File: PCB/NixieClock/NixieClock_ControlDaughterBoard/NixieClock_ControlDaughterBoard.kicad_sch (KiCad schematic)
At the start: 35 parts, among them J1 Conn_01x05, J2 Conn_01x05, J3 Conn_01x04_Pin, J4 Conn_01x04_Pin, Q1 IRLML6244, Q2 IRLML6244, Q3 IRLML6402

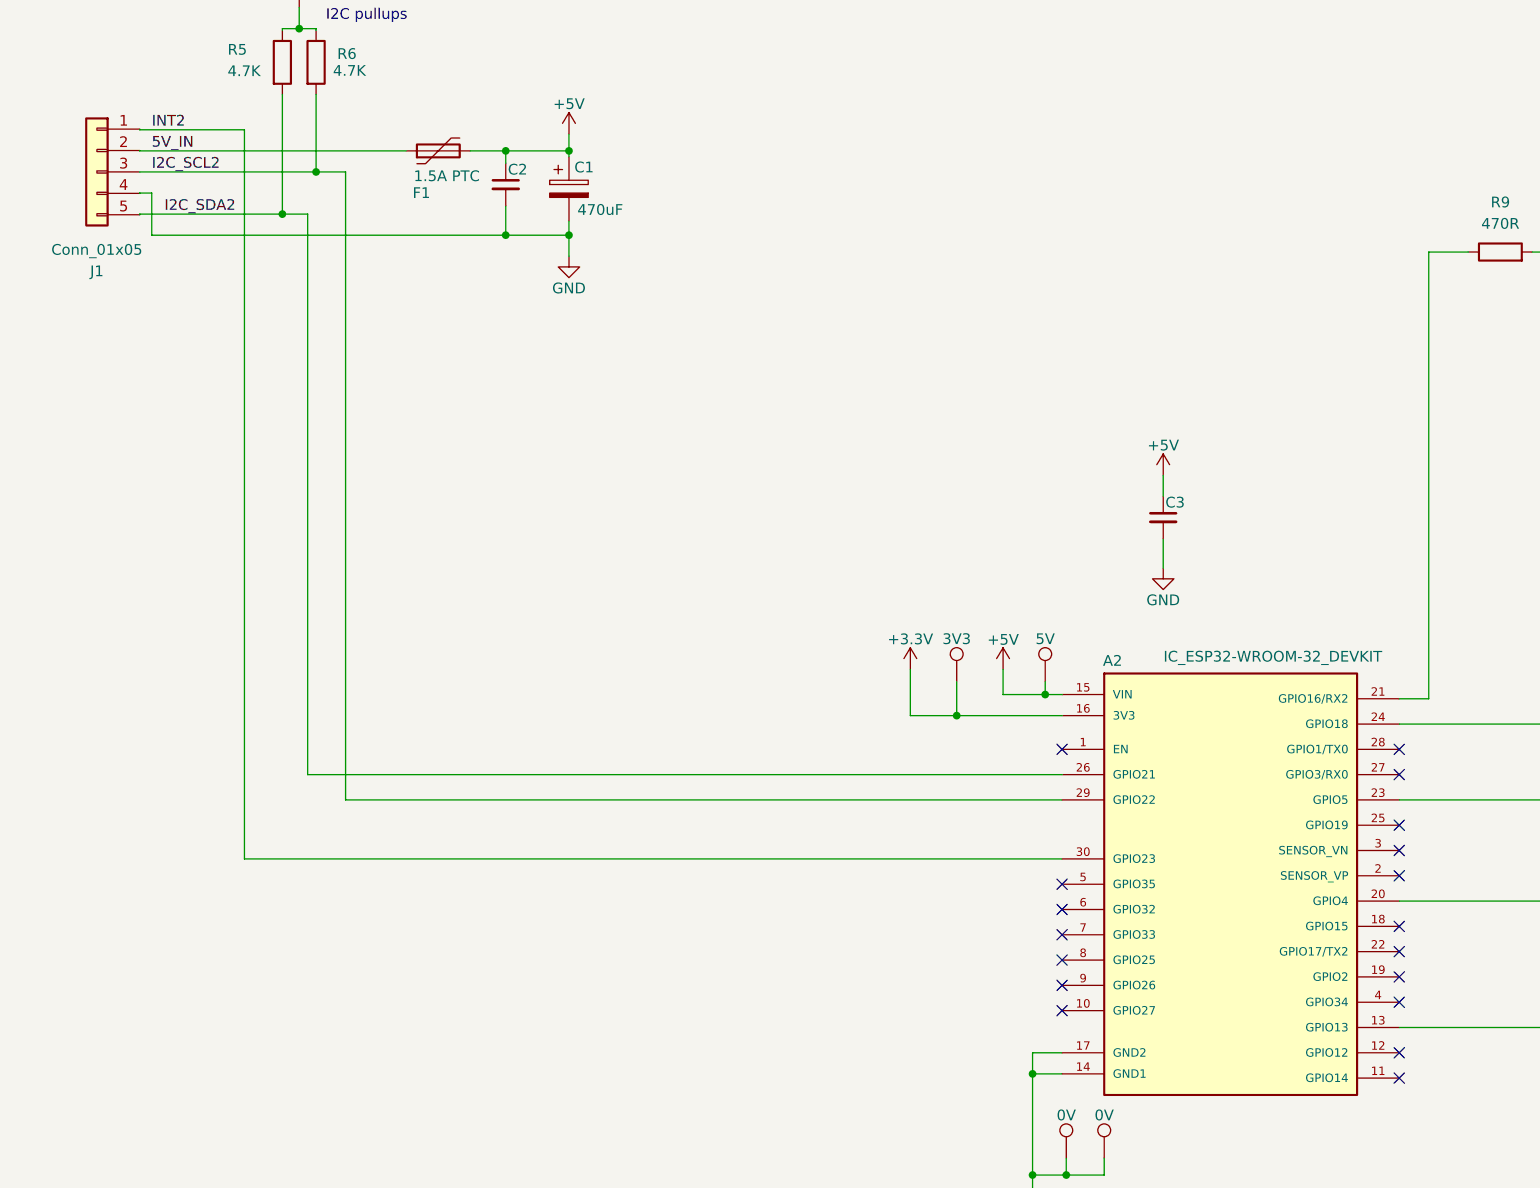
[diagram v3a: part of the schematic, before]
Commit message: PCB layout 2 complete
layout 1 was incorrect as the connectors and LEDs were not located in the right place to correctly mate with the tube panel PCBA. When connectors and LEDs were moved, all the traces became scrambled. it was necessary to re-wire the entire board.
ESP32 pins were also remapped to improve ease of wiring
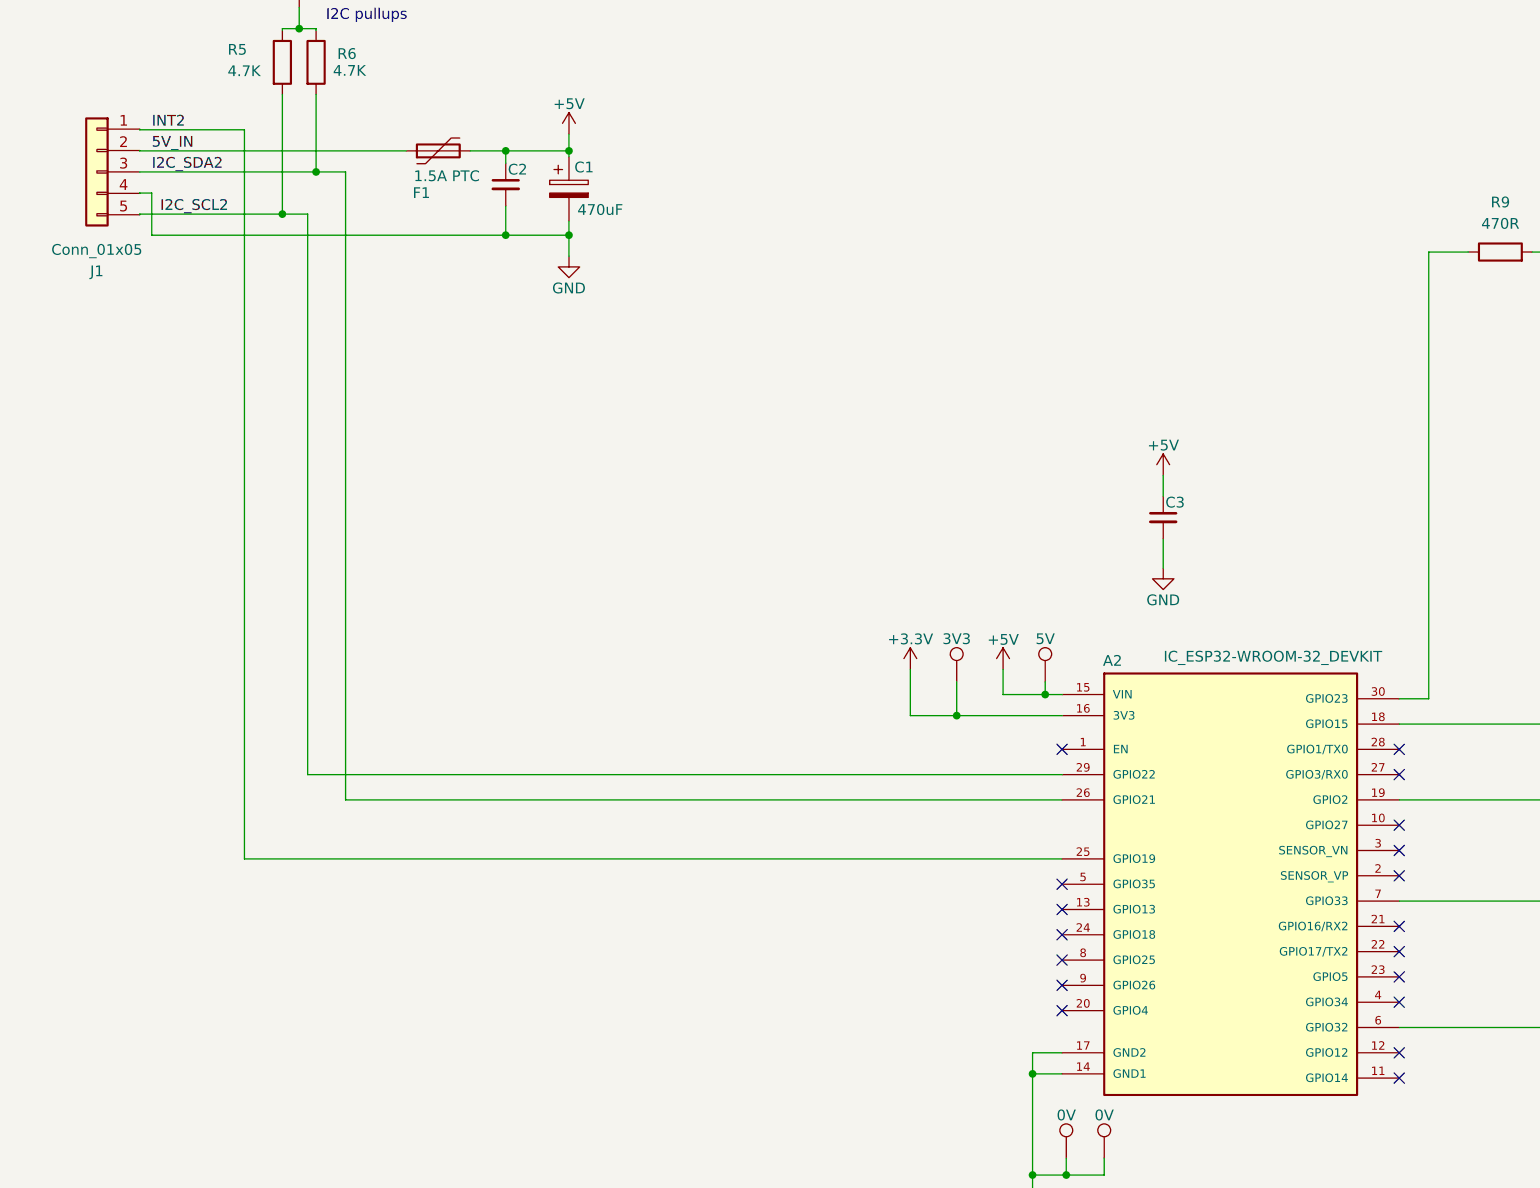
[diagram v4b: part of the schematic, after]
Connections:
- net I2C_SCL1: now also A2.18 (GPIO15); no longer A2.24 (GPIO18)
- net I2C_SCL2: now also J1.5 (Pin_5), R5.2; no longer J1.3 (Pin_3), R6.2
- net I2C_SDA1: now also A2.19 (GPIO2); no longer A2.23 (GPIO5)
- net I2C_SDA2: now also J1.3 (Pin_3), R6.2; no longer J1.5 (Pin_5), R5.2
- net INT2: now also A2.25 (GPIO19); no longer A2.30 (GPIO23)
- net LDR_IN: now also A2.7 (GPIO33); no longer A2.20 (GPIO4)
- net LED-Data_3V3: now also A2.6 (GPIO32); no longer A2.13 (GPIO13)
- net at R9.1: now also A2.30 (GPIO23); no longer A2.21 (GPIO16/RX2)
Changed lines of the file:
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@@
+		)
+	)
+	(label "I2C_SDA2"
+		(at 91 37 0)
+		(effects
+			(font
+				(size 1.27 1.27)
+			)
+			(justify left bottom)
 		)
 	)
@@
 	(label "INT2"
 		(at 91 32 0)
-		(effects
-			(font
-				(size 1.27 1.27)
-			)
-			(justify left bottom)
-		)
-	)
-	(label "I2C_SCL2"
-		(at 91 37 0)
 		(effects
 			(font
@@
 		)
 	)
-	(label "I2C_SCL1"
-		(at 352.5 142.5 0)
+	(label "I2C_SCL2"
+		(at 92 42 0)
 		(effects
 			(font
@@
 		)
 	)
-	(label "I2C_SDA2"
-		(at 92.5 42 0)
+	(label "I2C_SCL1"
+		(at 352.5 142.5 0)
 		(effects
 			(font

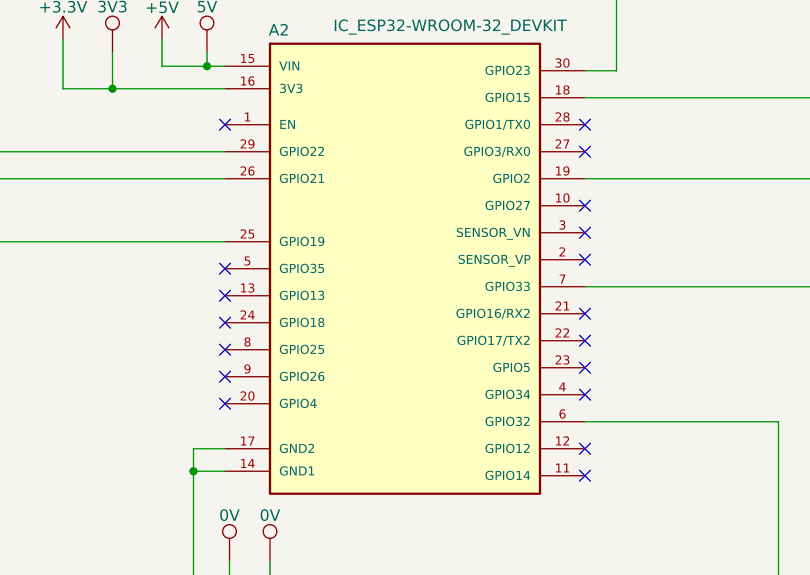
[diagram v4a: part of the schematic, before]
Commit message: I2C pin remap based on breadboard tests
tested I2C pin mappings on breadboard and found that using GPIO2 caused the board to get stuck in boot mode. remapped to adjacent pin GPIO4 for safety.
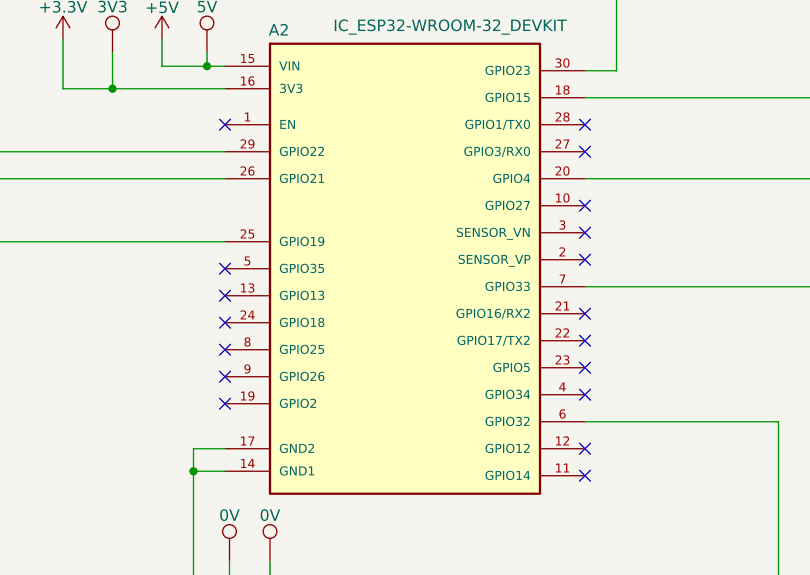
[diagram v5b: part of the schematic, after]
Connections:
- net I2C_SDA1: now also A2.20 (GPIO4); no longer A2.19 (GPIO2)

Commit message: Fill component details and export BOM
filled missing component information, exported BOM
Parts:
- A1: Manufacturer (none) -> Unknown; Manufacturer PN (none) -> ASSY_NCH8200HV; Supplier (none) -> Amazon
- A2: Manufacturer P/N ESP32-WROOM-32_DEVKIT -> (none); Manufacturer PN (none) -> ESP32-WROOM-32_DEVKIT; Supplier Terminal Curiosity -> Amazon
- A3: value ~ -> 4090; Manufacturer (none) -> Adafruit; Manufacturer PN (none) -> 4090; Supplier (none) -> Digikey
- C1: Manufacturer P/N UWT1C471MNL1GS -> (none); Manufacturer PN (none) -> UWT1C471MNL1GS
- C2, C3: Manufacturer P/N CL21B104KCFNNNE -> (none); Manufacturer PN (none) -> CL21B104KCFNNNE
- D1: Manufacturer (none) -> Generic; Manufacturer PN (none) -> PL9823
- D2, D3, D4: Manufacturer (none) -> Generic; Manufacturer PN (none) -> PL9823; Supplier (none) -> Terminal Curiosity
- F1: Manufacturer P/N NANOSMDC150F-2 -> (none); Manufacturer PN (none) -> NANOSMDC150F-2
- J1, J2: Manufacturer (none) -> JST Sales America Inc.; Manufacturer PN (none) -> B5B-XH-A; Supplier (none) -> Digikey
- J3, J4: value Conn_01x04_Pin -> Conn_01x04; Manufacturer (none) -> Sullins Connector Solutions; Manufacturer PN (none) -> PPTC041LFBN-RC; Supplier (none) -> Digikey
- Q1: Manufacturer PN (none) -> IRLML6244TRPBF
- Q2: Manufacturer P/N IRLML6344TRPBF -> (none); Manufacturer PN (none) -> IRLML6244TRPBF
- Q3: Manufacturer IRLML6402TRPBF -> Infineon; Manufacturer PN (none) -> IRLML6402TRPBF
- R1, R2, R5, R6: Manufacturer (none) -> Yageo; Manufacturer PN (none) -> RC0805JR-074K7L
- R15, R17, R4, R7, R8: Manufacturer (none) -> Yageo; Manufacturer PN (none) -> RC0805FR-1310KL
- R3, R9: Manufacturer P/N RC0805FR-07470RL -> (none); Manufacturer PN (none) -> RC0805FR-07470RL
- TP1, TP2, TP5, TP6: Manufacturer P/N RCUCTE -> (none); Manufacturer PN (none) -> RCUCTE

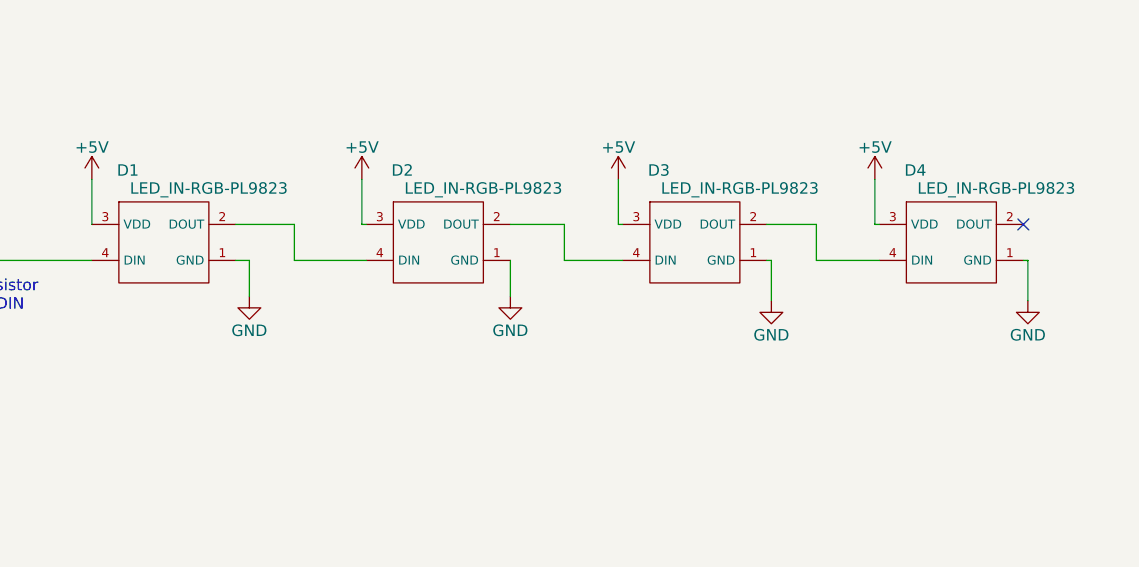
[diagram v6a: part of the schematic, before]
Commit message: swap pins 1,2 on LEDs
LED pin layout was mistakenly swapped. discovered on Rev01 prototype. swapped pins in the SCH and PCB files. updated assembly to Rev02
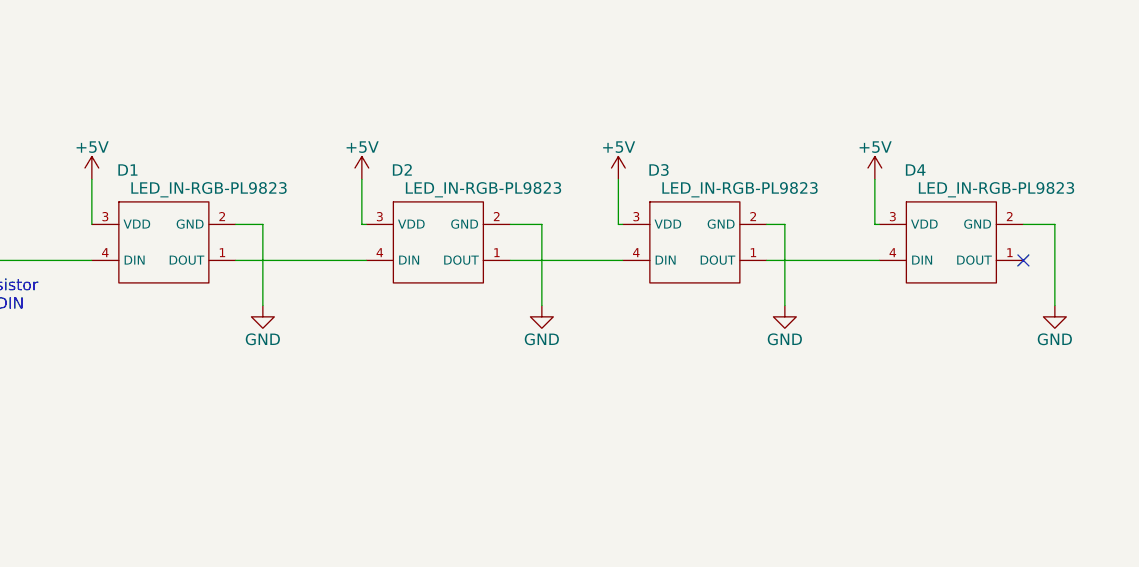
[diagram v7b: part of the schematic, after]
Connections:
- net GND: now also D1.2 (GND), D2.2 (GND), D3.2 (GND), D4.2 (GND); no longer D1.1 (GND), D2.1 (GND), D3.1 (GND), D4.1 (GND)
- net at D2.4 (DIN): now also D1.1 (DOUT); no longer D1.2 (DOUT)
- net at D4.4 (DIN): now also D3.1 (DOUT); no longer D3.2 (DOUT)
- net at D3.4 (DIN): now also D2.1 (DOUT); no longer D2.2 (DOUT)

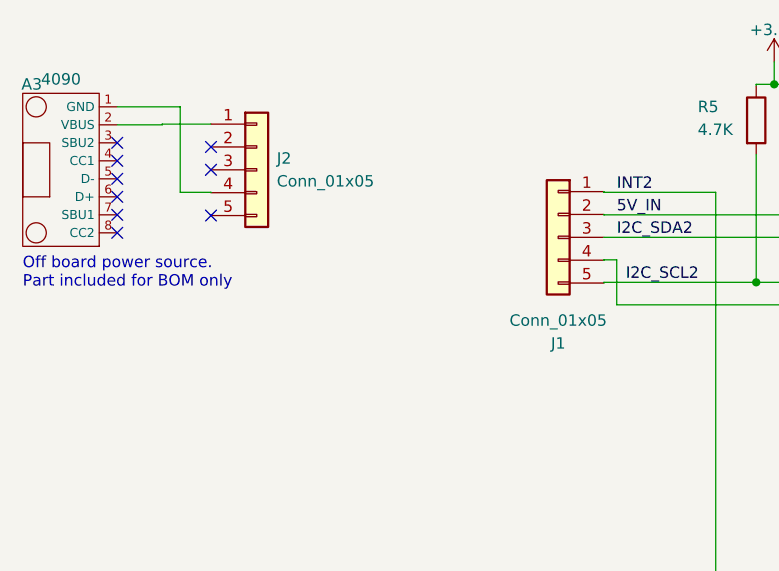
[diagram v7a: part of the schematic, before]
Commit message: fixed power in pin (1->2)
J2 5V pin was mistakenly wired to pin 1 instead of pin 2 (like on the control board connector J1)
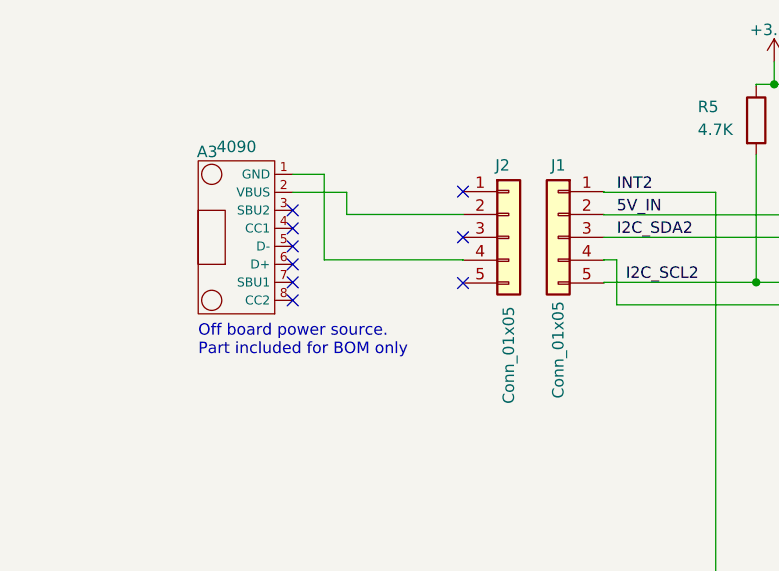
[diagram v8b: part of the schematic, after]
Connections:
- net at J2.1 (Pin_1): no longer A3.2 (VBUS)
- net at J2.2 (Pin_2): now also A3.2 (VBUS)
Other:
- moved on the sheet: A3, J2
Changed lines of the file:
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@@
 	(text "Off board power source.\nPart included for BOM only"
 		(exclude_from_sim no)
-		(at 25 41 0)
+		(at 44.5 48.5 0)
 		(effects
 			(font
@@
 	)
 	(no_connect
-		(at 45.92 34.58)
+		(at 73.92 42.08)
 	)
 	(no_connect
@@
 	)
 	(no_connect
-		(at 45.92 29.5)
+		(at 73.92 37)
 	)
 	(no_connect
-		(at 35.5 34.5)
+		(at 55 42)
 	)
 	(no_connect
@@
 	)
 	(no_connect
-		(at 45.92 26.96)
-	)
-	(no_connect
 		(at 239 144.5)
 	)
@@
 	)
 	(no_connect
-		(at 35.5 36.5)
+		(at 55 44)
 	)
 	(no_connect
@@
 	)
 	(no_connect
-		(at 35.5 28.5)
+		(at 55 36)
 	)
 	(no_connect
-		(at 35.5 32.5)
+		(at 55 40)
 	)
 	(no_connect
-		(at 35.5 26.5)
+		(at 73.92 31.92)
+	)
+	(no_connect
+		(at 55 34)
 	)
 	(no_connect
@@
 	)
 	(no_connect
-		(at 35.5 30.5)
+		(at 55 38)
 	)
 	(no_connect
@@
 	(wire
 		(pts
-			(xy 35.5 24.5) (xy 40.5 24.5)
-		)
-		(stroke
-			(width 0)
-			(type default)
-		)
-	)
-	(wire
-		(pts
 			(xy 91 39.5) (xy 91 44.5)
 		)
@@
 	(wire
 		(pts
-			(xy 45.92 32) (xy 45.92 32.04)
+			(xy 73.92 39.5) (xy 73.92 39.54)
 		)
 		(stroke
@@
 	(wire
 		(pts
+			(xy 73.92 34.46) (xy 61 34.46)
+		)
+		(stroke
+			(width 0)
+			(type default)
+		)
+	)
+	(wire
+		(pts
 			(xy 279 39) (xy 279 41.42)
 		)
@@
 	(wire
 		(pts
-			(xy 35.5 22.5) (xy 42.5 22.5)
+			(xy 55 30) (xy 58.5 30)
 		)
 		(stroke
@@
 	(wire
 		(pts
-			(xy 40.5 24.42) (xy 45.92 24.42)
+			(xy 61 32) (xy 55 32)
 		)
 		(stroke
@@
 	(wire
 		(pts
+			(xy 61 34.46) (xy 61 32)
+		)
+		(stroke
+			(width 0)
+			(type default)
+		)
+	)
+	(wire
+		(pts
 			(xy 341 126.5) (xy 345.5 126.5)
 		)
@@
 	(wire
 		(pts
-			(xy 42.5 32) (xy 45.92 32)
+			(xy 58.5 39.5) (xy 73.92 39.5)
 		)
 		(stroke
@@
 	(wire
 		(pts
-			(xy 42.5 22.5) (xy 42.5 32)
+			(xy 58.5 30) (xy 58.5 39.5)
 		)
 		(stroke
@@
 	(wire
 		(pts
-			(xy 40.5 24.5) (xy 40.5 24.42)
-		)
-		(stroke
-			(width 0)
-			(type default)
-		)
-	)
-	(wire
-		(pts
 			(xy 380 75.42) (xy 383.92 75.42)
 		)
@@
 	(symbol
 		(lib_id "Connector_Generic:Conn_01x05")
-		(at 51 29.5 0)
+		(at 79 37 0)
 		(unit 1)
 		(exclude_from_sim no)
@@
 		(on_board no)
 		(dnp no)
-		(fields_autoplaced yes)
 		(property "Reference" "J2"
-			(at 53.23 28.2299 0)
+			(at 77.5 29 0)
 			(effects
 				(font
@@
 		)
 		(property "Value" "Conn_01x05"
-			(at 53.23 30.7699 0)
+			(at 79 55.5 90)
 			(effects
 				(font
@@
 		)
 		(property "Footprint" "Connector_JST:JST_XH_B5B-XH-A_1x05_P2.50mm_Vertical"
-			(at 51 29.5 0)
+			(at 79 37 0)
 			(effects
 				(font
@@
 		)
 		(property "Datasheet" "~"
-			(at 51 29.5 0)
+			(at 79 37 0)
 			(effects
 				(font
@@
 		)
 		(property "Description" "CONN HEADER VERT 5POS 2.5MM"
-			(at 51 29.5 0)
+			(at 79 37 0)
 			(effects
 				(font
@@
 		)
 		(property "Company" ""
-			(at 51 29.5 0)
+			(at 79 37 0)
 			(effects
 				(font
@@
 		)
 		(property "Manufacturer" "JST Sales America Inc."
-			(at 51 29.5 0)
+			(at 79 37 0)
 			(effects
 				(font
@@
 		)
 		(property "Supplier" "Digikey"
-			(at 51 29.5 0)
+			(at 79 37 0)
 			(effects
 				(font
@@
 		)
 		(property "Manufacturer PN" "B5B-XH-A"
-			(at 51 29.5 0)
+			(at 79 37 0)
 			(effects
 				(font
@@
 	(symbol
 		(lib_id "TerminalCuriositySymbols:ASSY_USB-C-Breakout")
-		(at 33.5 21 180)
+		(at 53 28.5 180)
 		(unit 1)
 		(exclude_from_sim no)
@@
 		(dnp no)
 		(property "Reference" "A3"
-			(at 26 20 0)
+			(at 45.5 27.5 0)
 			(effects
 				(font
@@
 		)
 		(property "Value" "4090"
-			(at 29.25 19.44 0)
+			(at 48.75 26.94 0)
 			(effects
 				(font
@@
 		)
 		(property "Footprint" ""
-			(at 33.5 21 0)
+			(at 53 28.5 0)
 			(effects
 				(font
@@
 		)
 		(property "Datasheet" ""
-			(at 33.5 21 0)
+			(at 53 28.5 0)
 			(effects
 				(font
@@
 		)
 		(property "Description" "ADAFRUIT USB C BREAKOUT BOARD"
-			(at 33.5 21 0)
+			(at 53 28.5 0)
 			(effects
 				(font
@@
 		)
 		(property "Company" ""
-			(at 33.5 21 0)
+			(at 53 28.5 0)
 			(effects
 				(font
@@
 		)
 		(property "Manufacturer" "Adafruit"
-			(at 33.5 21 0)
+			(at 53 28.5 0)
 			(effects
 				(font
@@
 		)
 		(property "Supplier" "Digikey"
-			(at 33.5 21 0)
+			(at 53 28.5 0)
 			(effects
 				(font
@@
 		)
 		(property "Manufacturer PN" "4090"
-			(at 33.5 21 0)
+			(at 53 28.5 0)
 			(effects
 				(font
@@
 		(dnp no)
 		(property "Reference" "J1"
-			(at 84.5 48.78 0)
+			(at 84.5 29 0)
 			(effects
 				(font
@@
 		)
 		(property "Value" "Conn_01x05"
-			(at 84.5 46.24 0)
+			(at 84.5 49.5 90)
 			(effects
 				(font
